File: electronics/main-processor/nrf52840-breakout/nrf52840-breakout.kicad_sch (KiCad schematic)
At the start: 80 parts, among them J1 TBP02R2-381-03BE, J2 TBP02R2-381-02BE, J3 ST1W008S4AR1500, J4 TBP02R2-381-03BE, J5 Conn_01x03_Male, J6 CONUFL001-SMD-T, P1 USB_C_Plug, Q1 BSS214NW, Q2 AOD417, SW1 SW_DIP_x02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

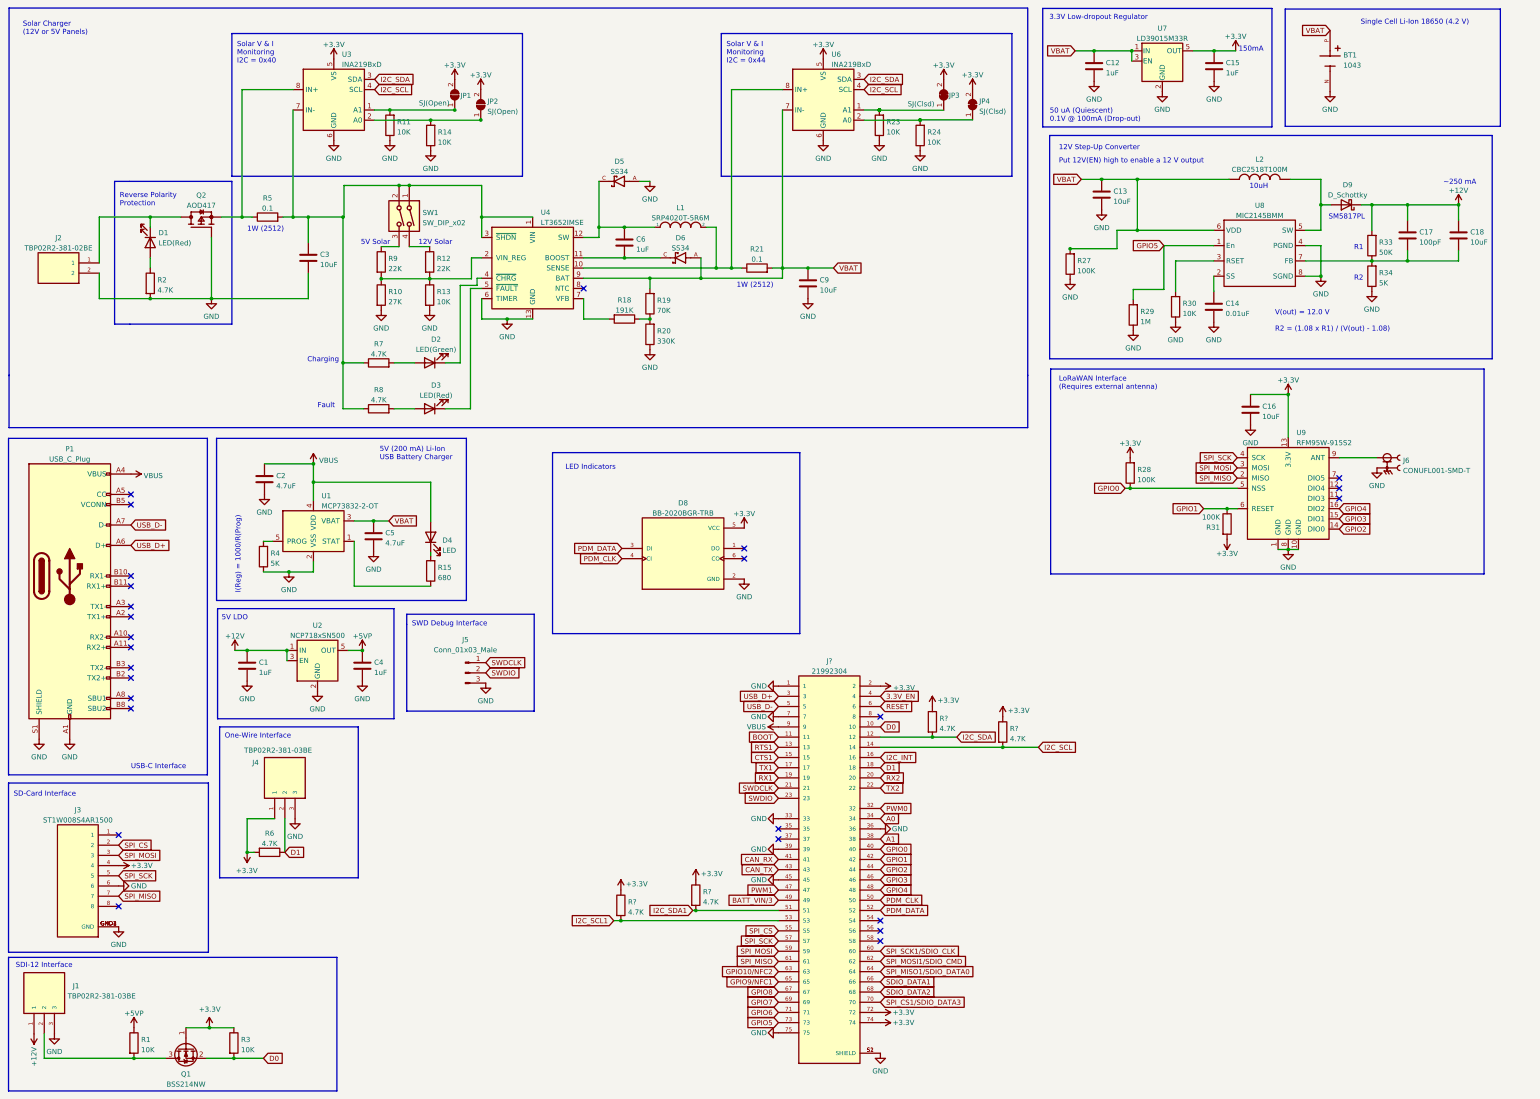
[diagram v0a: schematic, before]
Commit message: started on PCB for mainboard
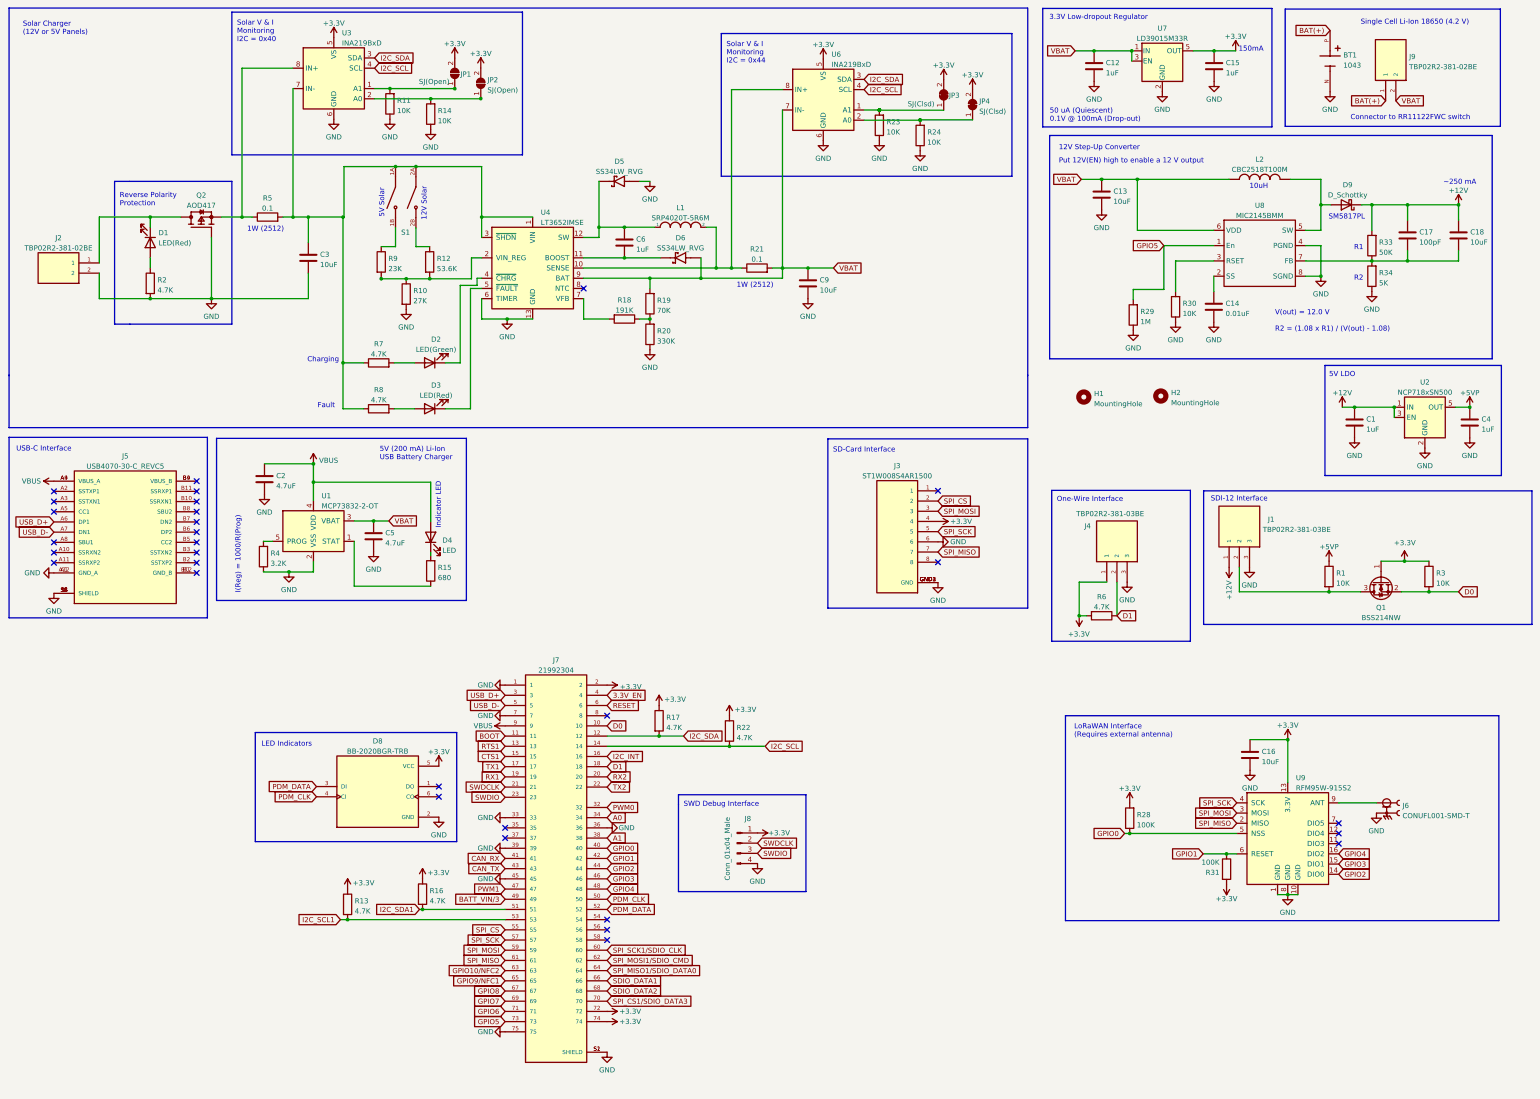
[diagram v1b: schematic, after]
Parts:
- removed D5, D6: SS34, DIOM7959X265N, symbol SS34:SS34
- removed J5: Conn_01x03_Male, symbol Connector:Conn_01x03_Male
- removed P1: USB_C_Plug, symbol Connector:USB_C_Plug
- removed R13: 10K, symbol Device:R
- removed R27: 100K, symbol Device:R
- removed SW1: SW_DIP_x02, symbol Switch:SW_DIP_x02
- added D5, D6: SS34LW_RVG, SS34LW_RVG:SODFL3718X102N, symbol SS34LW_RVG:SS34LW_RVG
- added H1, H2: MountingHole, MountingHole:MountingHole_3.2mm_M3_Pad_Via, symbol Mechanical:MountingHole
- added J5: USB4070-30-C_REVC5, USB4070-30-C:USB4070-30-C, symbol USB4070-30-C:USB4070-30-C_REVC5
- added J8: Conn_01x04_Male, Connector_PinHeader_2.54mm:PinHeader_1x04_P2.54mm_Vertical, symbol Connector:Conn_01x04_Male
- added J9: TBP02R2-381-02BE, TBP02R2-381-02BE:CUI_TBP02R2-381-02BE, symbol TBP02R2-381-02BE:TBP02R2-381-02BE
- added S1: DS04-254-2-02BK-SMT, DS04-254-2-02BK-SMT:SW_DS04-254-2-02BK-SMT, symbol DS04-254-2-02BK-SMT:DS04-254-2-02BK-SMT
- BT1: footprint BAT_1043 -> 1043:BAT_1043
- C1, C12, C13, C14, C15, C16, C17, C18, C2, C3, C4, C5, C6, C9: footprint (none) -> Capacitor_SMD:C_0805_2012Metric
- D1, D2, D3, D4: footprint (none) -> LED_SMD:LED_0805_2012Metric
- D8: footprint LED_BB-2020BGR-TRB -> BB-2020BGR-TRB:LED_BB-2020BGR-TRB
- D9: footprint (none) -> SM5817PL:SODFL3718X108N
- J1, J4: footprint CUI_TBP02R2-381-03BE -> TBP02R2-381-03BE:CUI_TBP02R2-381-03BE
- J2: footprint CUI_TBP02R2-381-02BE -> TBP02R2-381-02BE:CUI_TBP02R2-381-02BE
- J3: footprint JAE_ST1W008S4AR1500 -> ST1W008S4AR1500:JAE_ST1W008S4AR1500
- J6: footprint LINX_CONUFL001-SMD-T -> CONUFL001-SMD-T:LINX_CONUFL001-SMD-T
- J7: renamed from J?; footprint TE_21992304 -> 21992304:TE_21992304
- JP1, JP2: footprint (none) -> Jumper:SolderJumper-2_P1.3mm_Open_Pad1.0x1.5mm
- JP3, JP4: footprint (none) -> Jumper:SolderJumper-2_P1.3mm_Bridged_Pad1.0x1.5mm
- L1: footprint (none) -> SRP4020TA-5R6M:IND_SRP4020TA-5R6M
- L2: footprint INDC2518X200N -> CBC2518T100M:INDC2518X200N
- Q2: footprint DPAK228P994X240_3N -> AOD417:DPAK228P994X240_3N
- R1, R10, R11, R14, R15, R18, R19, R2, R20, R23, R24, R28, R29, R3, R30, R31, R33, R34, R6, R7, R8: footprint (none) -> Resistor_SMD:R_0805_2012Metric
- R12: value 22K -> 53.6K; footprint (none) -> Resistor_SMD:R_0805_2012Metric
- R13, R16, R17, R22: renamed from R?; footprint (none) -> Resistor_SMD:R_0805_2012Metric
- R21, R5: footprint (none) -> Resistor_SMD:R_2512_6332Metric
- R4: value 5K -> 3.2K; footprint (none) -> Resistor_SMD:R_0805_2012Metric
- R9: value 22K -> 23K; footprint (none) -> Resistor_SMD:R_0805_2012Metric
- U8: footprint (none) -> MIC2145BMM:MIC2145BMM
- U9: footprint (none) -> RFM95W-915S2:XCVR_RFM95W-915S2
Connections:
- net +3.3V: now also J8.1 (Pin_1)
- net GND: now also D5.A, J5.A1 (GND_A), J5.A12 (GND_A), J5.S1 (SHIELD), J5.S2 (SHIELD), J5.S3 (SHIELD), J5.S4 (SHIELD), J5.S5 (SHIELD), J5.S6 (SHIELD), J5.S7 (SHIELD), J5.S8 (SHIELD), J8.4 (Pin_4)
- net SWDCLK: now also J8.2 (Pin_2)
- net SWDIO: now also J8.3 (Pin_3)
- net USB_D+: now also J5.A6 (DP1)
- net USB_D-: now also J5.A7 (DN1)
- net VBAT: now also D6.A, J9.2; no longer BT1.P
- net VBUS: now also J5.A4 (VBUS_A), J5.A9 (VBUS_A)
- net at C6.1, L1.1, U4.12 (SW): now also D5.C
- net at C3.1, R5.2, R7.1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: now also S1.1A, S1.2A
- net at R9.1: now also S1.1B
- net at R12.1: now also S1.2B
- net at C6.2, U4.11 (BOOST): now also D6.C
- new net: J5.B1 (GND_B), J5.B12 (GND_B)
- new net: J5.B4 (VBUS_B), J5.B9 (VBUS_B)
- new net BAT(+): BT1.P, J9.1
- no-connect marks 26 -> 30
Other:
- note added: "Connector to RR11122FWC switch"
- note added: "Indicator LED"
- moved on the sheet: C1, C16, C4, D8, J1, J3, J4, J6, J7, JP1, JP2, Q1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

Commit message: up to pcb trace routing of circuit board, added boot and reset button
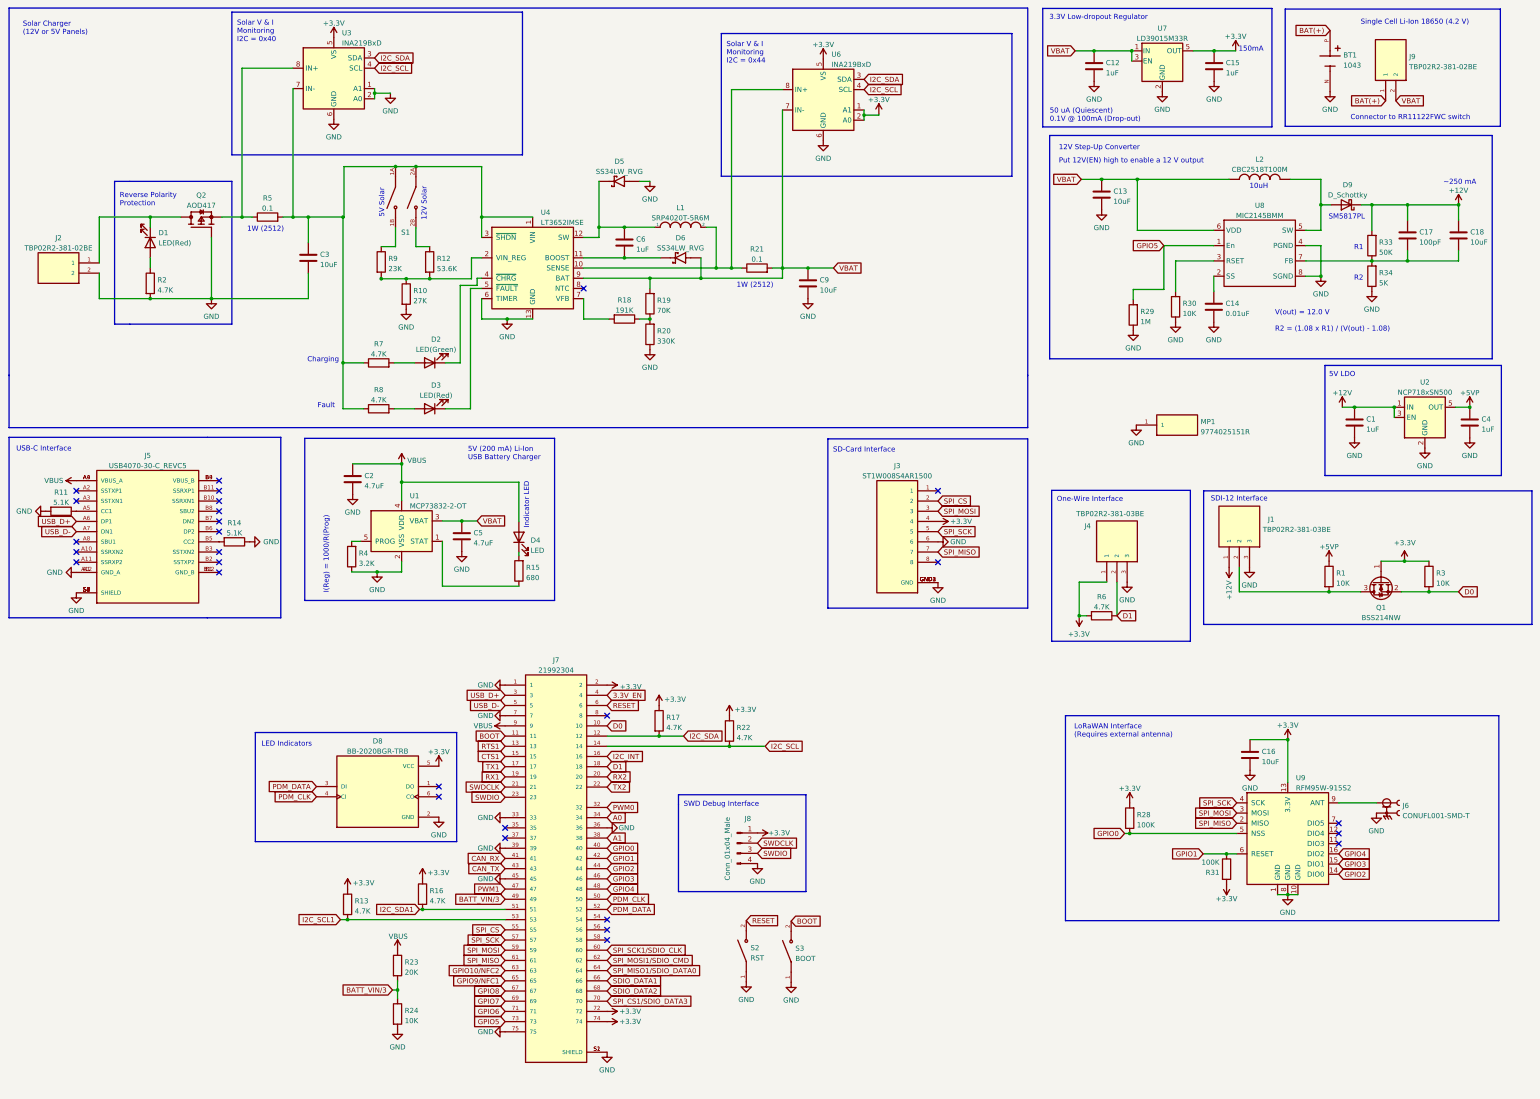
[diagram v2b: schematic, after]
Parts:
- removed H1, H2: MountingHole, MountingHole:MountingHole_3.2mm_M3_Pad_Via, symbol Mechanical:MountingHole
- removed JP1, JP2: SJ(Open), Jumper:SolderJumper-2_P1.3mm_Open_Pad1.0x1.5mm, symbol Jumper:SolderJumper_2_Open
- removed JP3, JP4: SJ(Clsd), Jumper:SolderJumper-2_P1.3mm_Bridged_Pad1.0x1.5mm, symbol Jumper:SolderJumper_2_Bridged
- added MP1: 9774025151R, 9774025151R:WE_9774025151R, symbol 9774025151R:9774025151R
- added S2: RST, PTS636_SM43J_SMTR_LFS:SW_PTS636_SM43J_SMTR_LFS, symbol PTS636_SM43J_SMTR_LFS:PTS636_SM43J_SMTR_LFS
- added S3: BOOT, PTS636_SM43J_SMTR_LFS:SW_PTS636_SM43J_SMTR_LFS, symbol PTS636_SM43J_SMTR_LFS:PTS636_SM43J_SMTR_LFS
- R11, R14: value 10K -> 5.1K
- R23: value 10K -> 20K
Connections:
- net +3.3V: now also U6.1 (A1), U6.2 (A0)
- net BATT_VIN/3: now also R23.2, R24.1
- net BOOT: now also S3.2
- net GND: now also R11.2, R24.2, U3.1 (A1), U3.2 (A0), MP1.1, S2.1, S3.1; no longer R11.1, R23.1, R24.1
- net RESET: now also S2.2
- net VBUS: now also R23.1
- net at R14.2: now also J5.B5 (CC2); no longer U3.2 (A0)
- net at J5.A5 (CC1): now also R11.1
- no-connect marks 30 -> 28
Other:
- moved on the sheet: C2, C5, D4, J5, R15, R4, U1
